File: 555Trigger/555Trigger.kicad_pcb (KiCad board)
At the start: 2 copper layers, 9 parts, among them SW1 SW_DPDT_x2, U2 TLC555xP

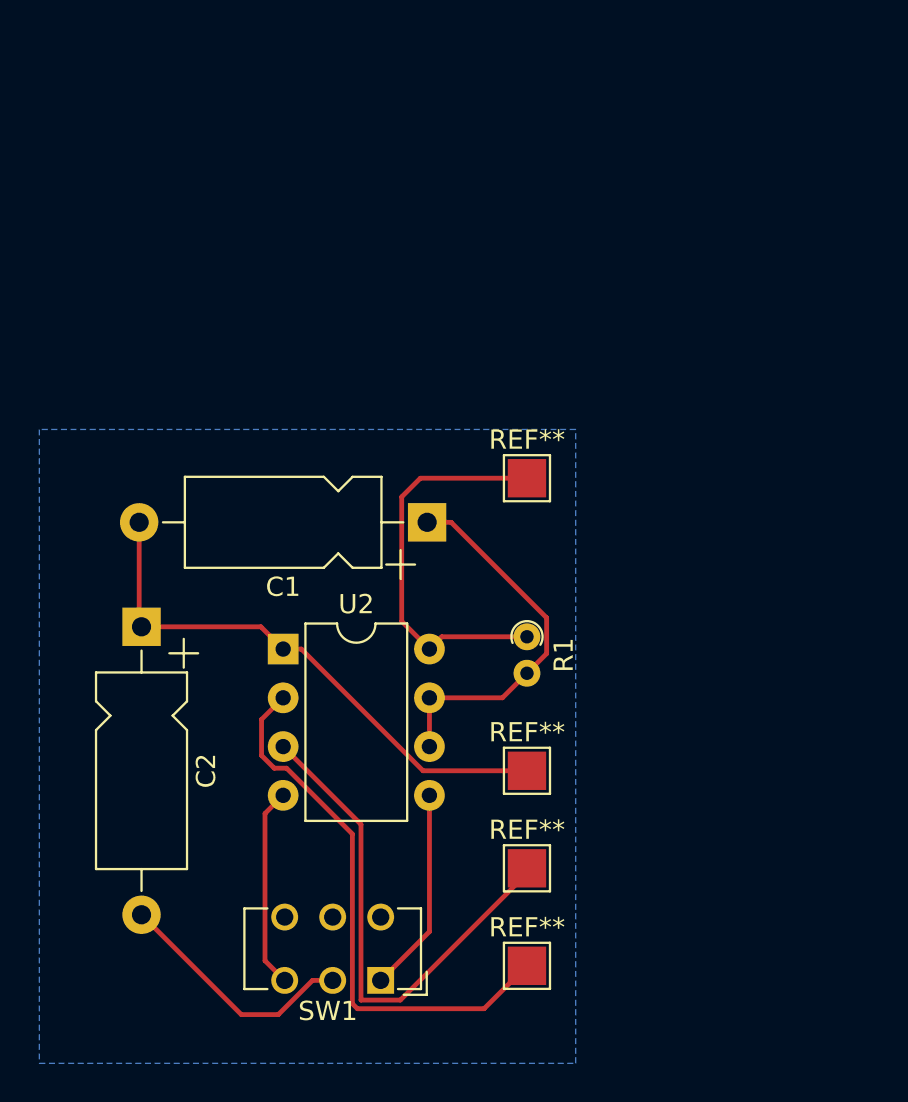
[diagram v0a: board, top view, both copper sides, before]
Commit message: added filtering and buffers to circuit todo: make one large master control board
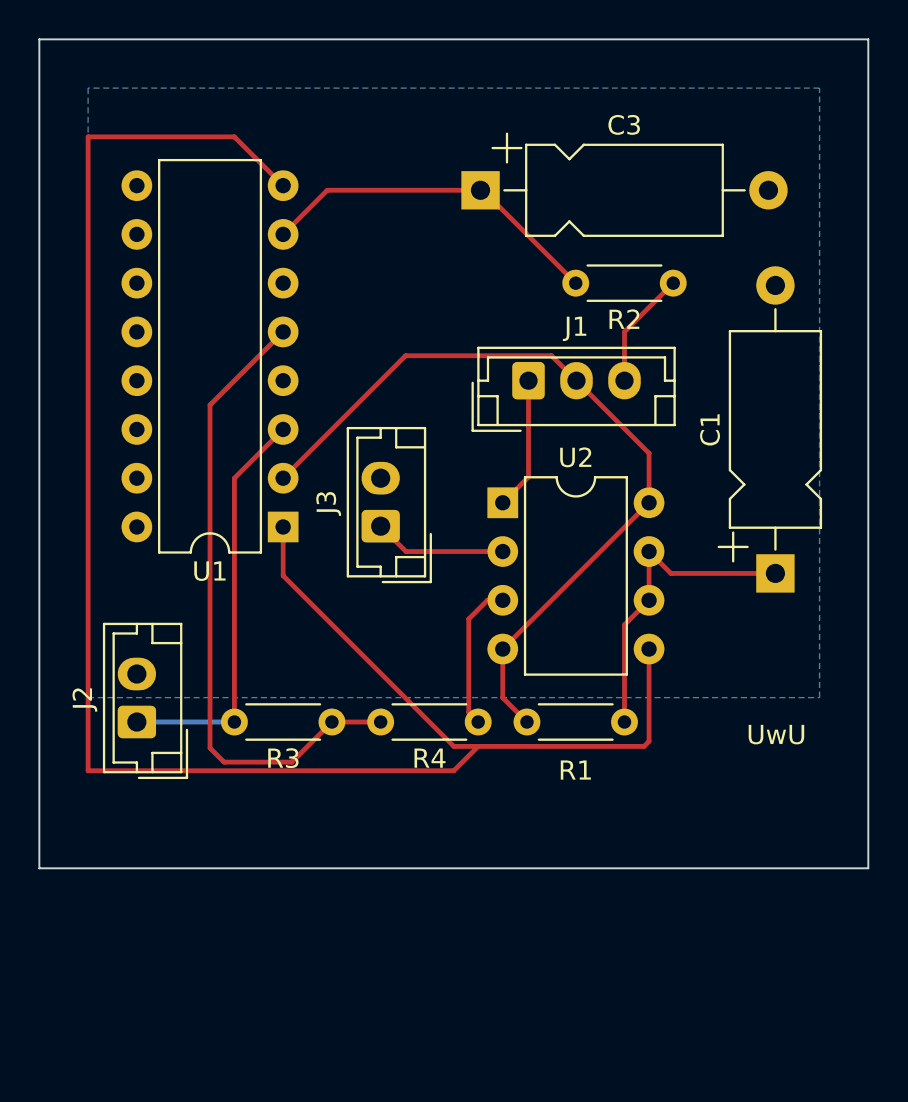
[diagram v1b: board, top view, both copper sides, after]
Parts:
- removed C2: 0.1 μF, Capacitor_THT:CP_Axial_L10.0mm_D4.5mm_P15.00mm_Horizontal
- removed REF** (x4): TestPoint_Pad_2.0x2.0mm, TestPoint:TestPoint_Pad_2.0x2.0mm
- removed SW1: SW_DPDT_x2, Button_Switch_THT:SW_CuK_JS202011CQN_DPDT_Straight
- added C3: C, Capacitor_THT:CP_Axial_L10.0mm_D4.5mm_P15.00mm_Horizontal, F.Cu at (83.9, 30.7)
- added J1: Conn_01x03_Socket, Connector_JST:JST_EH_B3B-EH-A_1x03_P2.50mm_Vertical, F.Cu at (86.4, 40.6)
- added J2: Timing Signal Out, Connector_JST:JST_EH_B2B-EH-A_1x02_P2.50mm_Vertical, F.Cu at (66.0, 58.4)
- added J3: Timing Signal In, Connector_JST:JST_EH_B2B-EH-A_1x02_P2.50mm_Vertical, F.Cu at (78.7, 48.2)
- added R2: R, Resistor_THT:R_Axial_DIN0204_L3.6mm_D1.6mm_P5.08mm_Horizontal, F.Cu at (94.0, 35.6)
- added R3: 1K, Resistor_THT:R_Axial_DIN0204_L3.6mm_D1.6mm_P5.08mm_Horizontal, F.Cu at (76.2, 58.4)
- added R4: 1K, Resistor_THT:R_Axial_DIN0204_L3.6mm_D1.6mm_P5.08mm_Horizontal, F.Cu at (83.8, 58.4)
- added U1: L272, Package_DIP:DIP-16_W7.62mm, F.Cu at (73.7, 48.3)
- R1: footprint Resistor_THT:R_Axial_DIN0204_L3.6mm_D1.6mm_P1.90mm_Vertical -> Resistor_THT:R_Axial_DIN0204_L3.6mm_D1.6mm_P5.08mm_Horizontal
- moved C1 18.3 mm to (99.3, 50.7), turned to 90 degrees
- moved U2 13.7 mm to (85.1, 47.0)
- moved R1 4.44 mm to (86.4, 58.4), turned to 0 degrees
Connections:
- U2 pad 2: VBUS -> Net-(J3-Pin_1)
- U2 pad 3: VAA -> Net-(U2-Q)
- U2 pad 4: Net-(SW1A-C) -> +5V
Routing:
- net Net-(U1A--): track 10.7 -> 95.2 mm
- net Net-(U1B--): track 0.00 -> 33.3 mm
- net VBUS: track 28.9 -> 0.00 mm
- net VAA: track 26.5 -> 0.00 mm
- net GND: track 28.7 -> 6.96 mm
- net Net-(J2-Pin_1): track 0.00 -> 21.4 mm
- net +5V: track 20.8 -> 41.5 mm
- net Net-(U1A-+): track 0.00 -> 18.2 mm
- net Net-(SW1A-B): track 12.8 -> 0.00 mm
- net Net-(SW1A-C): track 10.5 -> 0.00 mm
- net Net-(U2-Q): track 0.00 -> 7.75 mm
- net Net-(J3-Pin_1): track 0.00 -> 6.91 mm
- net Net-(J1-Pin_3): track 0.00 -> 6.13 mm
- net Net-(U2-DIS): track 20.0 -> 16.5 mm
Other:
- board outline added: 43.2 x 43.2 mm
- board text added: "UwU"

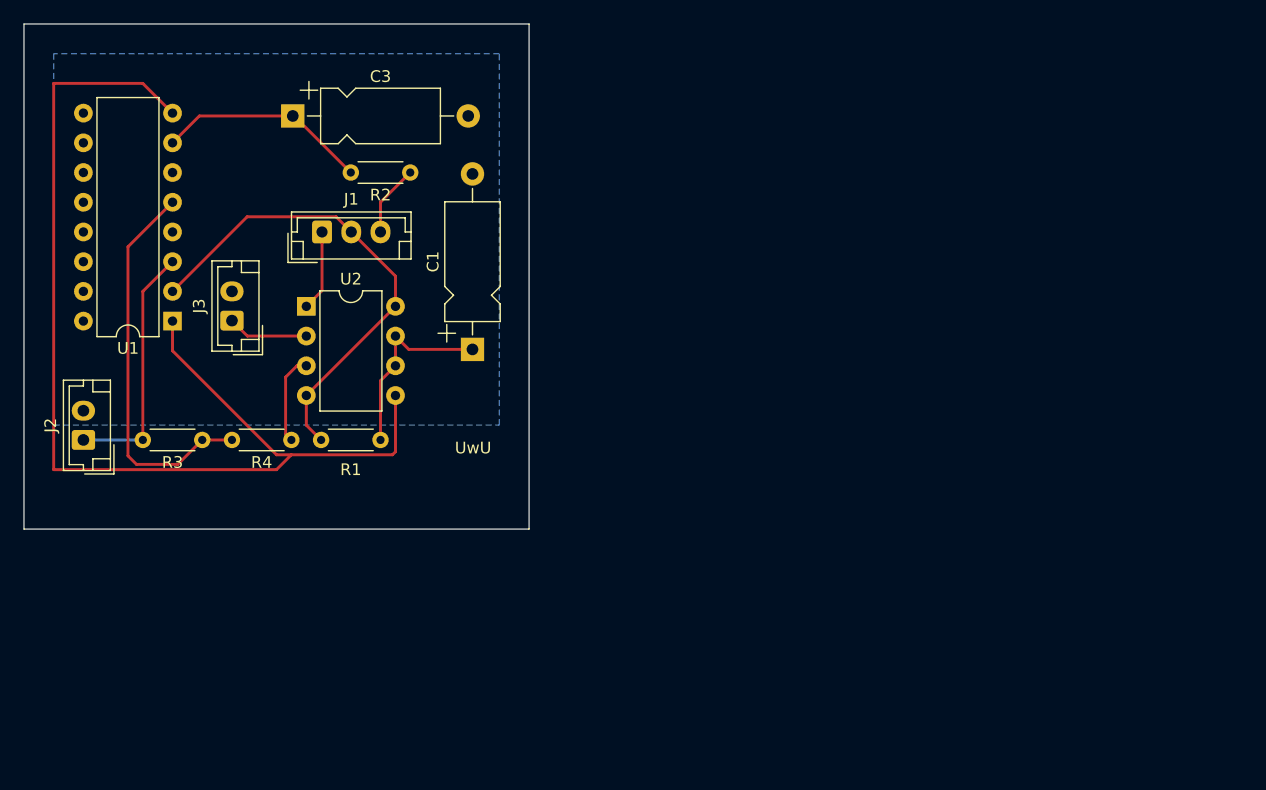
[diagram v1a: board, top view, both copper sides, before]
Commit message: changed to SMD
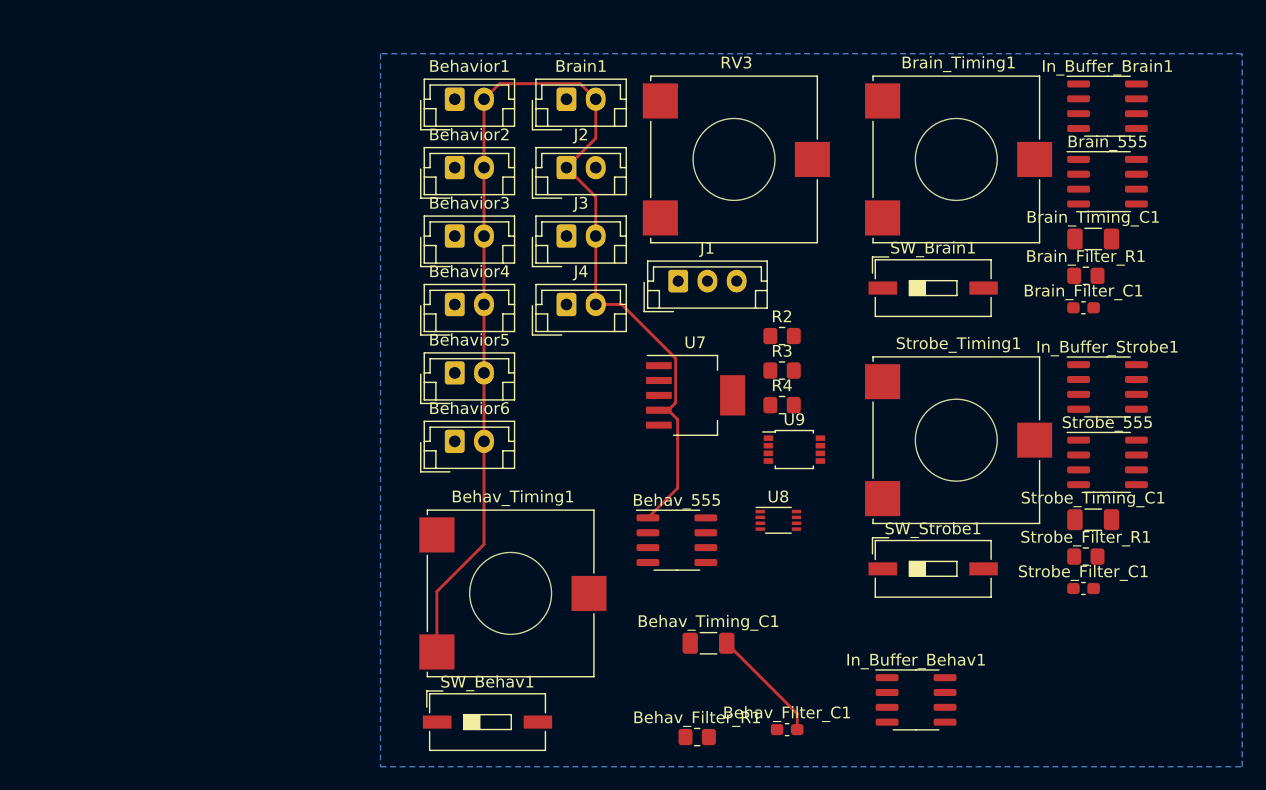
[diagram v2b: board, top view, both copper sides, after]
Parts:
- removed C1: 2.2 μF, Capacitor_THT:CP_Axial_L10.0mm_D4.5mm_P15.00mm_Horizontal
- removed C3: C, Capacitor_THT:CP_Axial_L10.0mm_D4.5mm_P15.00mm_Horizontal
- removed R1: 1k, Resistor_THT:R_Axial_DIN0204_L3.6mm_D1.6mm_P5.08mm_Horizontal
- removed U1: L272, Package_DIP:DIP-16_W7.62mm
- removed U2: TLC555xP, Package_DIP:DIP-8_W7.62mm
- added Behav_555: ~, Package_SO:SOIC-8_3.9x4.9mm_P1.27mm, F.Cu at (116.8, 67.0)
- added Behav_Filter_C1: 10 pF, Capacitor_SMD:C_0603_1608Metric_Pad1.08x0.95mm_HandSolder, F.Cu at (126.2, 83.2)
- added Behav_Filter_R1: 32k, Resistor_SMD:R_0805_2012Metric_Pad1.20x1.40mm_HandSolder, F.Cu at (118.5, 83.8)
- added Behav_Timing1: 0-10k, Potentiometer_SMD:Potentiometer_ACP_CA14-VSMD_Vertical_Hole, F.Cu at (102.8, 71.5)
- added Behav_Timing_C1: 1.7u, Capacitor_SMD:C_1206_3216Metric_Pad1.33x1.80mm_HandSolder, F.Cu at (119.5, 75.8)
- added Behavior1: Conn_01x02_Socket, Connector_JST:JST_EH_B2B-EH-A_1x02_P2.50mm_Vertical, F.Cu at (97.8, 29.3)
- added Behavior2: Conn_01x02_Socket, Connector_JST:JST_EH_B2B-EH-A_1x02_P2.50mm_Vertical, F.Cu at (97.8, 35.1)
- added Behavior3: Conn_01x02_Socket, Connector_JST:JST_EH_B2B-EH-A_1x02_P2.50mm_Vertical, F.Cu at (97.8, 41.0)
- added Behavior4: Conn_01x02_Socket, Connector_JST:JST_EH_B2B-EH-A_1x02_P2.50mm_Vertical, F.Cu at (97.8, 46.8)
- added Behavior5: Conn_01x02_Socket, Connector_JST:JST_EH_B2B-EH-A_1x02_P2.50mm_Vertical, F.Cu at (97.8, 52.7)
- added Behavior6: Conn_01x02_Socket, Connector_JST:JST_EH_B2B-EH-A_1x02_P2.50mm_Vertical, F.Cu at (97.8, 58.5)
- added Brain1: Conn_01x02_Socket, Connector_JST:JST_EH_B2B-EH-A_1x02_P2.50mm_Vertical, F.Cu at (107.3, 29.3)
- added Brain_555: ~, Package_SO:SOIC-8_3.9x4.9mm_P1.27mm, F.Cu at (153.6, 36.3)
- added Brain_Filter_C1: 10 pF, Capacitor_SMD:C_0603_1608Metric_Pad1.08x0.95mm_HandSolder, F.Cu at (151.5, 47.1)
- added Brain_Filter_R1: 32k, Resistor_SMD:R_0805_2012Metric_Pad1.20x1.40mm_HandSolder, F.Cu at (151.7, 44.4)
- added Brain_Timing1: 0-10k, Potentiometer_SMD:Potentiometer_ACP_CA14-VSMD_Vertical_Hole, F.Cu at (140.9, 34.4)
- added Brain_Timing_C1: 1.7u, Capacitor_SMD:C_1206_3216Metric_Pad1.33x1.80mm_HandSolder, F.Cu at (152.4, 41.2)
- added In_Buffer_Behav1: OPA333xxD, Package_SO:SOIC-8_3.9x4.9mm_P1.27mm, F.Cu at (137.2, 80.6)
- added In_Buffer_Brain1: OPA333xxD, Package_SO:SOIC-8_3.9x4.9mm_P1.27mm, F.Cu at (153.6, 29.9)
- added In_Buffer_Strobe1: OPA333xxD, Package_SO:SOIC-8_3.9x4.9mm_P1.27mm, F.Cu at (153.6, 53.9)
- added J4: Strobing_LED_2, Connector_JST:JST_EH_B2B-EH-A_1x02_P2.50mm_Vertical, F.Cu at (107.3, 46.8)
- added RV3: 10k, Potentiometer_SMD:Potentiometer_ACP_CA14-VSMD_Vertical_Hole, F.Cu at (121.9, 34.4)
- added SW_Behav1: SW_DIP_x01, Button_Switch_SMD:SW_DIP_SPSTx01_Slide_9.78x4.72mm_W8.61mm_P2.54mm, F.Cu at (100.6, 82.5)
- added SW_Brain1: SW_DIP_x01, Button_Switch_SMD:SW_DIP_SPSTx01_Slide_9.78x4.72mm_W8.61mm_P2.54mm, F.Cu at (138.7, 45.4)
- added SW_Strobe1: SW_DIP_x01, Button_Switch_SMD:SW_DIP_SPSTx01_Slide_9.78x4.72mm_W8.61mm_P2.54mm, F.Cu at (138.7, 69.4)
- added Strobe_555: ~, Package_SO:SOIC-8_3.9x4.9mm_P1.27mm, F.Cu at (153.6, 60.3)
- added Strobe_Filter_C1: 10 pF, Capacitor_SMD:C_0603_1608Metric_Pad1.08x0.95mm_HandSolder, F.Cu at (151.5, 71.1)
- added Strobe_Filter_R1: 32k, Resistor_SMD:R_0805_2012Metric_Pad1.20x1.40mm_HandSolder, F.Cu at (151.7, 68.4)
- added Strobe_Timing1: 0-10k, Potentiometer_SMD:Potentiometer_ACP_CA14-VSMD_Vertical_Hole, F.Cu at (140.9, 58.4)
- added Strobe_Timing_C1: 1.7u, Capacitor_SMD:C_1206_3216Metric_Pad1.33x1.80mm_HandSolder, F.Cu at (152.4, 65.2)
- added U7: 74LVC2G74, Package_TO_SOT_SMD:SOT-223-6_TabPin3, F.Cu at (118.4, 54.6)
- added U8: 74AHC2G00, Package_SO:VSSOP-8_2.3x2mm_P0.5mm, F.Cu at (125.5, 65.3)
- added U9: OPA2333xxD, Package_SO:OnSemi_Micro8, F.Cu at (126.8, 59.2)
- J2: value Timing Signal Out -> Conn_01x02_Socket
- J3: value Timing Signal In -> Strobing_LED_1
- R2: value R -> 10k; footprint Resistor_THT:R_Axial_DIN0204_L3.6mm_D1.6mm_P5.08mm_Horizontal -> Resistor_SMD:R_0805_2012Metric_Pad1.20x1.40mm_HandSolder
- R3, R4: value 1K -> 20k; footprint Resistor_THT:R_Axial_DIN0204_L3.6mm_D1.6mm_P5.08mm_Horizontal -> Resistor_SMD:R_0805_2012Metric_Pad1.20x1.40mm_HandSolder
- moved R3 49.9 mm to (125.8, 52.5), turned to 0 degrees
- moved J2 47.4 mm to (107.3, 35.1), turned to 0 degrees
- moved R4 42.1 mm to (125.8, 55.4), turned to 0 degrees
- moved R2 34.7 mm to (125.8, 49.5), turned to 0 degrees
- moved J1 30.7 mm to (116.9, 44.8)
- moved J3 29.5 mm to (107.3, 41.0), turned to 0 degrees
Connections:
- J1 pad 1: GND -> /Strobing_Trigger/CV_In
- J1 pad 2: +5V -> /Behavior_Camera_Unit/CV_In
- J1 pad 3: Net-(J1-Pin_3) -> /Brain_Camera_Unit/CV_In
- J2 pad 1: Net-(J2-Pin_1) -> GND
- J2 pad 2: GND -> +5V
- R2 pad 1: Net-(J1-Pin_3) -> +5V
- R2 pad 2: Net-(U1A-+) -> Net-(U9A-+)
- R3 pad 1: Net-(U1B--) -> Net-(U9A-+)
- R3 pad 2: Net-(J2-Pin_1) -> GND
- R4 pad 2: Net-(U1B--) -> GND
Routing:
- net GND: track 6.96 -> 113.9 mm
- net Net-(U1A--): track 95.2 -> 0.00 mm
- net +5V: track 41.5 -> 0.00 mm
- net Net-(U1B--): track 33.3 -> 0.00 mm
- net Net-(J2-Pin_1): track 21.4 -> 0.00 mm
- net Net-(U1A-+): track 18.2 -> 0.00 mm
- net Net-(U2-DIS): track 16.5 -> 0.00 mm
- net Net-(R4-Pad1): track 7.75 -> 0.00 mm
- net Net-(J3-Pin_1): track 6.91 -> 0.00 mm
- net Net-(J1-Pin_3): track 6.13 -> 0.00 mm
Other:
- board outline removed
- board text removed: "UwU"
